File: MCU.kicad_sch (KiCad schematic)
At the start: 16 parts, among them J1 2169900001, J3 Conn_01x06, SW3 SW_Push, SW4 SW_Push, SW5 SW_Push, SW6 SW_Push, SW7 SW_Push, U3 NORA-B106-00B, U7 FAN5622SX, U8 ESDR0502NMUTBG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

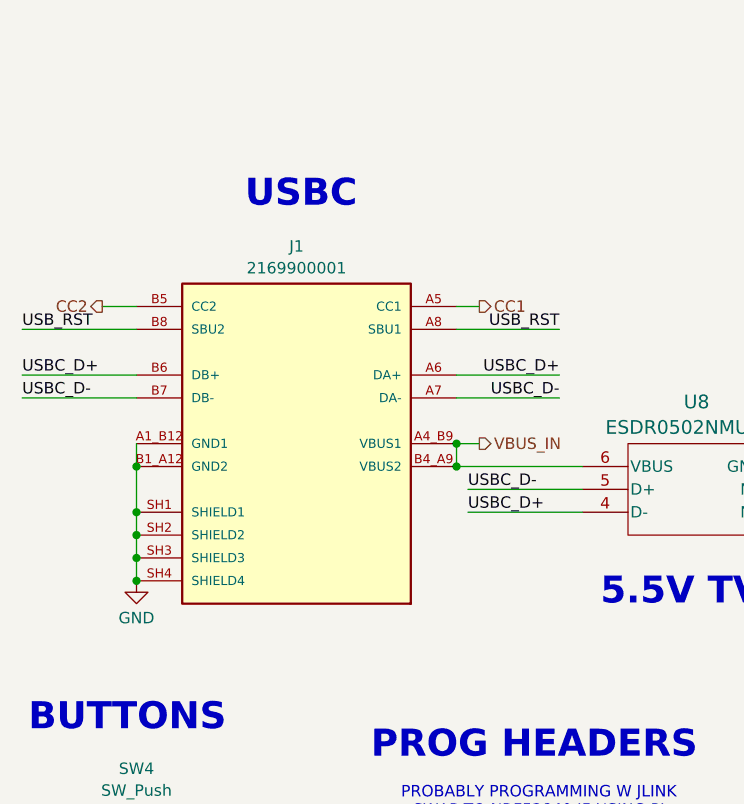
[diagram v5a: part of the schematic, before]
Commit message: Added Test Points and Changed to Top Mounted USBC
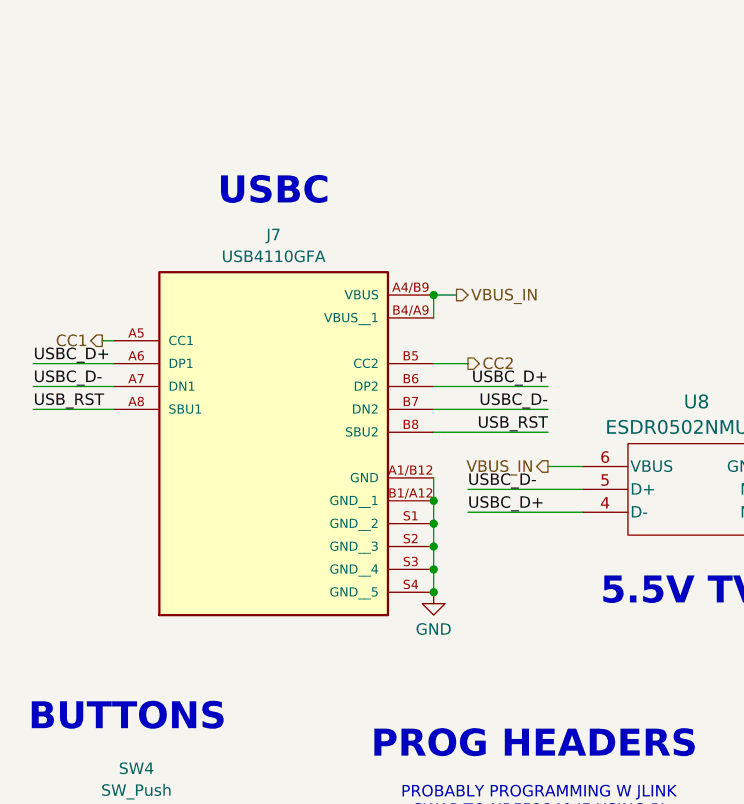
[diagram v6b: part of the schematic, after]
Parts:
- removed J1: 2169900001, Smart_Watch:MOLEX_2169900001, symbol Smart_Watch:2169900001
- added J7: USB4110GFA, Smart_Watch:GCT_USB4110GFA, symbol Smart_Watch:USB4110GFA
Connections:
- net CC1: now also J7.A5 (CC1)
- net CC2: now also J7.B5 (CC2)
- net GND: now also J7.A1/B12 (GND), J7.B1/A12 (GND__1), J7.S1 (GND__2), J7.S2 (GND__3), J7.S3 (GND__4), J7.S4 (GND__5)
- net USBC_D+: now also J7.A6 (DP1), J7.B6 (DP2)
- net USBC_D-: now also J7.A7 (DN1), J7.B7 (DN2)
- net USB_RST: now also J7.A8 (SBU1), J7.B8 (SBU2)
- net VBUS_IN: now also J7.A4/B9 (VBUS), J7.B4/A9 (VBUS__1)

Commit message: :)
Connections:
- no-connect marks 17 -> 18
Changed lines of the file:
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@@
+	)
+	(no_connect
+		(at 172.72 83.82)
 	)
 	(no_connect

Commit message: Fix some ERC problems
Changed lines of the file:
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@@
 	)
 	(junction
+		(at 58.42 104.14)
+		(diameter 0)
+		(color 0 0 0 0)
+	)
+	(junction
 		(at 172.72 144.78)
 		(diameter 0)
@@
 	)
 	(junction
-		(at 58.42 104.14)
+		(at 172.72 167.64)
 		(diameter 0)
 		(color 0 0 0 0)
 	)
 	(junction
-		(at 172.72 167.64)
+		(at 261.62 101.6)
 		(diameter 0)
 		(color 0 0 0 0)
 	)
 	(junction
-		(at 261.62 101.6)
+		(at 172.72 175.26)
 		(diameter 0)
 		(color 0 0 0 0)
 	)
 	(junction
-		(at 172.72 175.26)
+		(at 62.23 104.14)
 		(diameter 0)
 		(color 0 0 0 0)
@@
 	(wire
 		(pts
-			(xy 60.96 104.14) (xy 58.42 104.14)
+			(xy 66.04 104.14) (xy 62.23 104.14)
 		)
 		(stroke
@@
 	(wire
 		(pts
+			(xy 62.23 104.14) (xy 58.42 104.14)
+		)
+		(stroke
+			(width 0)
+			(type default)
+		)
+	)
+	(wire
+		(pts
 			(xy 99.06 49.53) (xy 99.06 45.72)
 		)
@@
 	(hierarchical_label "VBUS_IN"
 		(shape output)
-		(at 60.96 104.14 0)
+		(at 66.04 104.14 0)
 		(effects
 			(font
@@
 		)
 		(property "Footprint" "Smart_Watch:UDFN6_517AA_ONS-L"
-			(at 95.758 150.876 0)
+			(at 87.63 116.6325 0)
 			(hide yes)
-			(show_name yes)
+			(show_name no)
 			(do_not_autoplace no)
 			(effects
@@
 		)
 		(property "Datasheet" "ESDR0502NMUTBG"
-			(at 95.758 150.876 0)
+			(at 87.63 119.0568 0)
 			(hide yes)
-			(show_name yes)
+			(show_name no)
 			(do_not_autoplace no)
 			(effects
@@
 			(at 87.122 155.194 0)
 			(hide yes)
-			(show_name yes)
-			(do_not_autoplace no)
-			(effects
-				(font
-					(size 1.27 1.27)
-				)
-			)
-		)
-		(property "Check_prices" ""
-			(at 87.63 125.73 0)
-			(hide yes)
-			(show_name no)
-			(do_not_autoplace no)
-			(effects
-				(font
-					(size 1.27 1.27)
-				)
-			)
-		)
-		(property "Description_1" ""
-			(at 87.63 125.73 0)
-			(hide yes)
-			(show_name no)
-			(do_not_autoplace no)
-			(effects
-				(font
-					(size 1.27 1.27)
-				)
-			)
-		)
-		(property "Inductance" ""
-			(at 87.63 125.73 0)
-			(hide yes)
-			(show_name no)
-			(do_not_autoplace no)
-			(effects
-				(font
-					(size 1.27 1.27)
-				)
-			)
-		)
-		(property "MF" ""
-			(at 87.63 125.73 0)
-			(hide yes)
-			(show_name no)
-			(do_not_autoplace no)
-			(effects
-				(font
-					(size 1.27 1.27)
-				)
-			)
-		)
-		(property "MP" ""
-			(at 87.63 125.73 0)
-			(hide yes)
-			(show_name no)
-			(do_not_autoplace no)
-			(effects
-				(font
-					(size 1.27 1.27)
-				)
-			)
-		)
-		(property "Purchase-URL" ""
-			(at 87.63 125.73 0)
-			(hide yes)
-			(show_name no)
-			(do_not_autoplace no)
-			(effects
-				(font
-					(size 1.27 1.27)
-				)
-			)
-		)
-		(property "SnapEDA_Link" ""
-			(at 87.63 125.73 0)
-			(hide yes)
 			(show_name no)
 			(do_not_autoplace no)
@@
 	)
 	(symbol
+		(lib_id "power:PWR_FLAG")
+		(at 62.23 104.14 0)
+		(unit 1)
+		(body_style 1)
+		(exclude_from_sim no)
+		(in_bom yes)
+		(on_board yes)
+		(in_pos_files yes)
+		(dnp no)
+		(fields_autoplaced yes)
+		(property "Reference" "#FLG02"
+			(at 62.23 102.235 0)
+			(hide yes)
+			(show_name no)
+			(do_not_autoplace no)
+			(effects
+				(font
+					(size 1.27 1.27)
+				)
+			)
+		)
+		(property "Value" "PWR_FLAG"
+			(at 62.23 100.0069 0)
+			(show_name no)
+			(do_not_autoplace no)
+			(effects
+				(font
+					(size 1.27 1.27)
+				)
+			)
+		)
+		(property "Footprint" ""
+			(at 62.23 104.14 0)
+			(hide yes)
+			(show_name no)
+			(do_not_autoplace no)
+			(effects
+				(font
+					(size 1.27 1.27)
+				)
+			)
+		)
+		(property "Datasheet" ""
+			(at 62.23 104.14 0)
+			(hide yes)
+			(show_name no)
+			(do_not_autoplace no)
+			(effects
+				(font
+					(size 1.27 1.27)
+				)
+			)
+		)
+		(property "Description" "Special symbol for telling ERC where power comes from"
+			(at 62.23 104.14 0)
+			(hide yes)
+			(show_name no)
+			(do_not_autoplace no)
+			(effects
+				(font
+					(size 1.27 1.27)
+				)
+			)
+		)
+		(pin "1"
+		)
+		(instances
+			(project "Smart_Watch"
+				(path "/69095a4d-0a57-4fa3-aecb-1cfd89eedc11/bed567dd-6d09-419a-b99a-3e57c9439bd4/30bd5bb3-3a33-4afa-baf2-7512abedf580"
+					(reference "#FLG02")
+					(unit 1)
+				)
+			)
+		)
+	)
+	(symbol
 		(lib_id "power:GND")
 		(at 241.3 114.3 0)
@@
 			(do_not_autoplace no)
 			(effects
-				(font
-					(size 1.27 1.27)
-				)
-			)
-		)
-		(property "Check_prices" ""
-			(at 212.09 137.16 0)
-			(hide yes)
-			(show_name no)
-			(do_not_autoplace no)
-			(effects
-				(font
-					(size 1.27 1.27)
-				)
-			)
-		)
-		(property "Description_1" ""
-			(at 212.09 137.16 0)
-			(hide yes)
-			(show_name no)
-			(do_not_autoplace no)
-			(effects
-				(font
-					(size 1.27 1.27)
-				)
-			)
-		)
-		(property "Inductance" ""
-			(at 212.09 137.16 0)
-			(hide yes)
-			(show_name no)
-			(do_not_autoplace no)
-			(effects
-				(font
-					(size 1.27 1.27)
-				)
-			)
-		)
-		(property "MF" ""
-			(at 212.09 137.16 0)
-			(hide yes)
-			(show_name no)
-			(do_not_autoplace no)
-			(effects
-				(font
-					(size 1.27 1.27)
-				)
-			)
-		)
-		(property "MP" ""
-			(at 212.09 137.16 0)
-			(hide yes)
-			(show_name no)
-			(do_not_autoplace no)
-			(effects
-				(font
-					(size 1.27 1.27)
-				)
-			)
-		)
-		(property "Purchase-URL" ""
-			(at 212.09 137.16 0)
-			(hide yes)
-			(show_name no)
-			(do_not_autoplace no)
-			(effects
-				(font
-					(size 1.27 1.27)
-				)
-			)
-		)
-		(property "SnapEDA_Link" ""
-			(at 212.09 137.16 0)
-			(hide yes)
-			(show_name no)
-			(do_not_autoplace no)
-			(effects
